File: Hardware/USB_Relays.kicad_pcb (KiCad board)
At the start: 2 copper layers, 90 parts, among them J1 282834-3, J10 282834-3, J11 282834-3, J12 282834-3, J13 282834-3, J14 282834-3, J15 282834-3, J16 282834-3, J17 DNP, J18 2411_06, J2 282834-3, J3 282834-3, J4 282834-3, J5 282834-3, J6 282834-3, J7 282834-3, J8 282834-3, J9 282834-3, K1 HRS1H-S_DC5V, K10 HRS1H-S_DC5V, K11 HRS1H-S_DC5V, K12 HRS1H-S_DC5V, K13 HRS1H-S_DC5V, K14 HRS1H-S_DC5V, K15 HRS1H-S_DC5V, K16 HRS1H-S_DC5V, K2 HRS1H-S_DC5V, K3 HRS1H-S_DC5V, K4 HRS1H-S_DC5V, K5 HRS1H-S_DC5V, K6 HRS1H-S_DC5V, K7 HRS1H-S_DC5V, K8 HRS1H-S_DC5V, K9 HRS1H-S_DC5V, Q1 BC848, Q10 BC848, Q11 BC848, Q12 BC848, Q13 BC848, Q14 BC848, Q15 BC848, Q16 BC848, Q2 BC848, Q3 BC848, Q4 BC848, Q5 BC848, Q6 BC848, Q7 BC848, Q8 BC848, Q9 BC848, U1 PIC16F18854-SO, U2 FT230XS

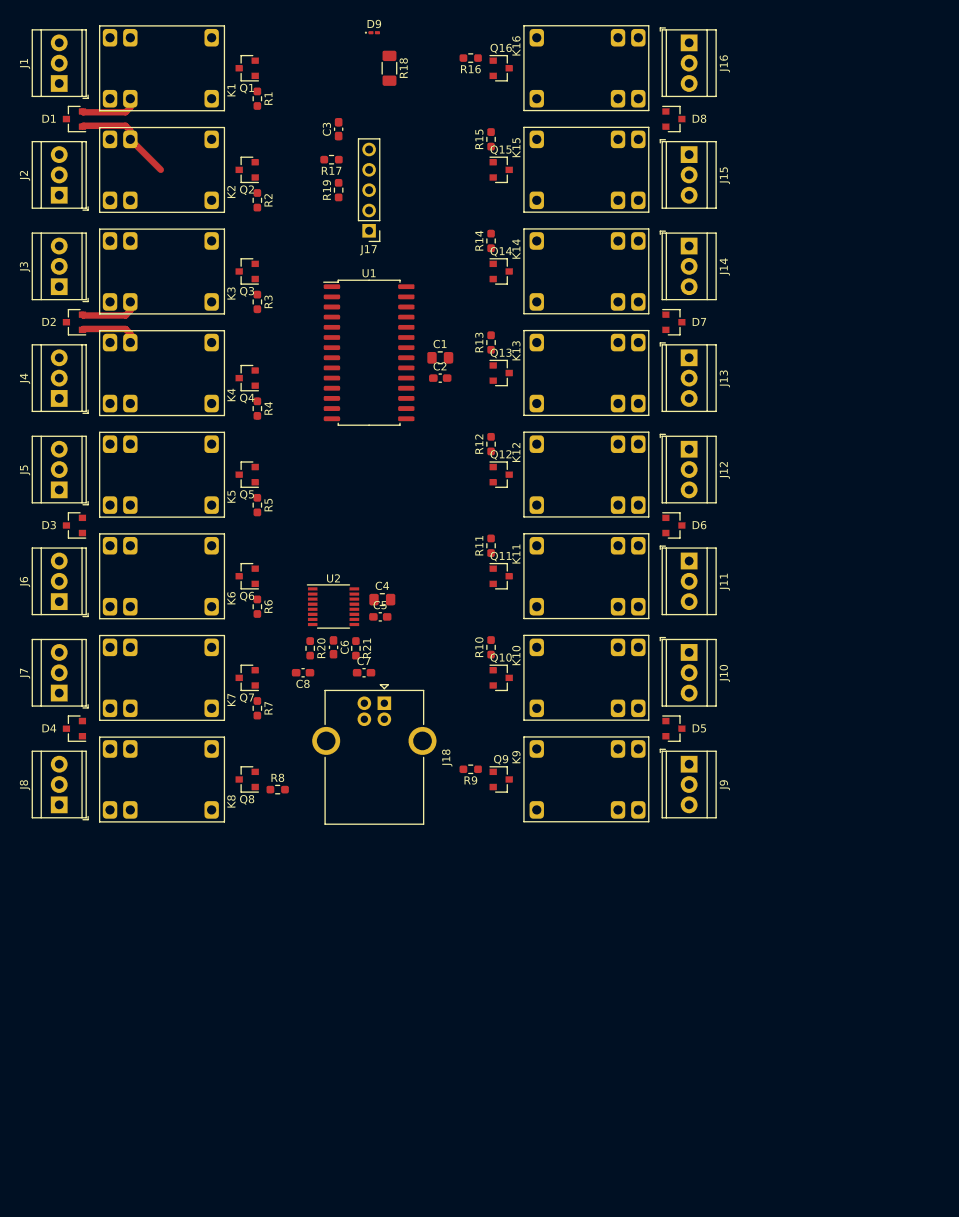
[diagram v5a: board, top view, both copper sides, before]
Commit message: [Hardware] Added mounting holes, PCB contour and ground planes.
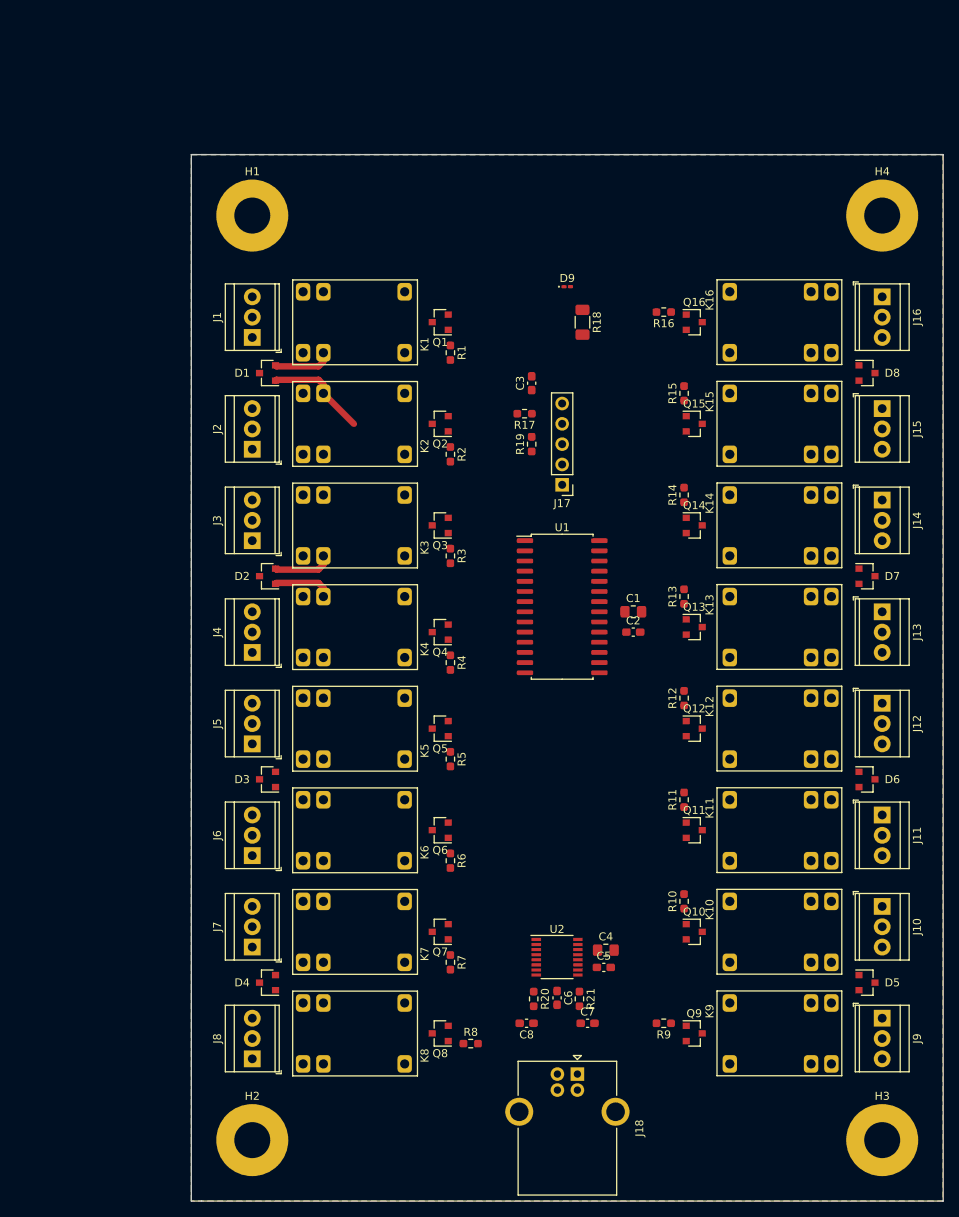
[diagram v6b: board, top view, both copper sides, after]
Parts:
- added H1: MountingHole_Pad, MountingHole:MountingHole_4.5mm_Pad, F.Cu at (45.7, 40.6)
- added H2: MountingHole_Pad, MountingHole:MountingHole_4.5mm_Pad, F.Cu at (45.7, 156.2)
- added H3: MountingHole_Pad, MountingHole:MountingHole_4.5mm_Pad, F.Cu at (124.5, 156.2)
- added H4: MountingHole_Pad, MountingHole:MountingHole_4.5mm_Pad, F.Cu at (124.5, 40.6)
- moved J18 52.3 mm to (86.4, 148.0)
- moved C4 52.0 mm to (89.9, 132.5)
- moved C5 52.0 mm to (89.7, 134.6)
- moved C6 52.0 mm to (83.8, 138.4)
- moved U2 52.0 mm to (83.8, 133.3)
- moved C7 52.0 mm to (87.6, 141.6)
- moved C8 52.0 mm to (80.0, 141.6)
- moved R20 52.0 mm to (80.9, 138.6)
- moved R21 52.0 mm to (86.6, 138.6)
- moved K10 39.9 mm to (111.8, 130.2)
- moved Q10 39.9 mm to (101.0, 130.2)
- moved J7 39.9 mm to (45.7, 132.1)
- moved J8 39.9 mm to (45.7, 146.1)
- moved K7 39.9 mm to (58.4, 130.2)
- moved Q7 39.9 mm to (69.2, 130.2)
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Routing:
- added copper zone on B.Cu, net GND
- added copper zone on F.Cu, net GND
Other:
- board outline added: 94 x 130.8 mm

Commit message: [Hardware] Routed whole PCB.
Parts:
- D9: footprint LED_SMD:LED_0201_0603Metric_Pad0.64x0.40mm_HandSolder -> LED_SMD:LED_0603_1608Metric_Pad1.05x0.95mm_HandSolder
- moved R13 6.63 mm to (97.8, 94.6), turned to 270 degrees
- moved C4 5.08 mm to (89.9, 127.4)
- moved C5 5.08 mm to (89.7, 129.5)
- moved C6 5.08 mm to (83.8, 133.3)
- moved C7 5.08 mm to (87.6, 136.5)
- moved C8 5.08 mm to (80.0, 136.5)
- moved R20 5.08 mm to (80.9, 133.5)
- moved R21 5.08 mm to (86.6, 133.5)
- moved U2 5.08 mm to (83.8, 128.3)
- moved R15 4.58 mm to (97.2, 66.7), turned to 270 degrees
- moved R5 4.32 mm to (72.5, 104.8), turned to 90 degrees
- moved R4 4.15 mm to (72.1, 92.7), turned to 90 degrees
- moved R12 4.13 mm to (96.8, 103.9), turned to 180 degrees
- moved R6 3.96 mm to (73.2, 118.4), turned to 0 degrees
- moved R7 3.87 mm to (73.0, 131.1), turned to 0 degrees
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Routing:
- net +5V: track 0.00 -> 686.7 mm, vias 0 -> 2
- net RELAY_8: track 0.00 -> 52.5 mm
- net RELAY_9: track 0.00 -> 47.8 mm
- net RELAY_7: track 0.00 -> 43.9 mm
- net RELAY_14: track 0.00 -> 39.7 mm, vias 0 -> 2
- net FTDI_RX: track 0.00 -> 39.4 mm, vias 0 -> 2
- net Net-(R18-Pad2): track 0.00 -> 39.1 mm, vias 0 -> 2
- net FTDI_TX: track 0.00 -> 38.9 mm, vias 0 -> 2
- net RELAY_10: track 0.00 -> 38.8 mm
- net RELAY_16: track 0.00 -> 36.6 mm
- net RELAY_11: track 0.00 -> 34.2 mm
- net RELAY_6: track 0.00 -> 33.6 mm
- net RELAY_1: track 0.00 -> 30.1 mm
- net RELAY_15: track 0.00 -> 25.5 mm
- net Net-(D7-Pad2): track 0.00 -> 22.6 mm
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- added copper zone on F.Cu, net +3.3VA
- added copper zone on F.Cu, net +5V

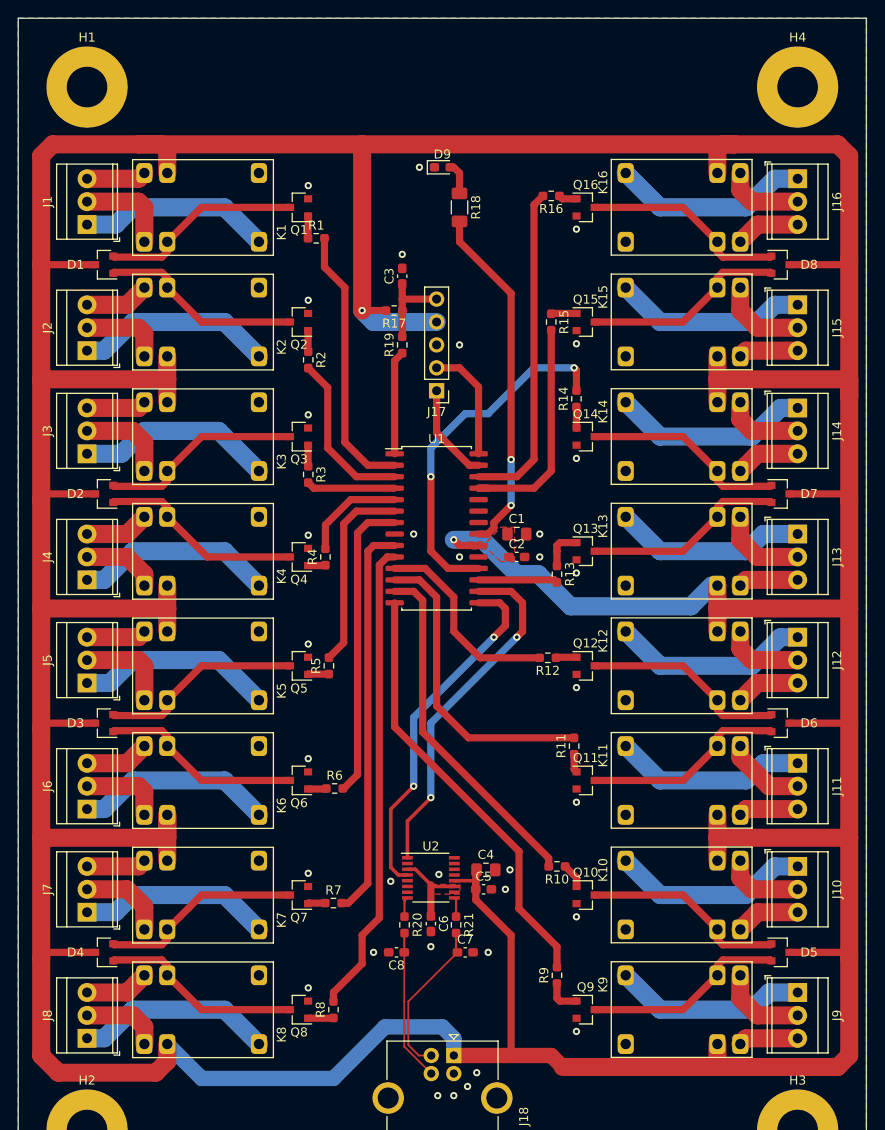
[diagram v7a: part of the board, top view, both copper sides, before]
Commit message: [Hardware] Moved LED to make it more visible, cleaned components designation positions, added information about connectors pins to the PCB.
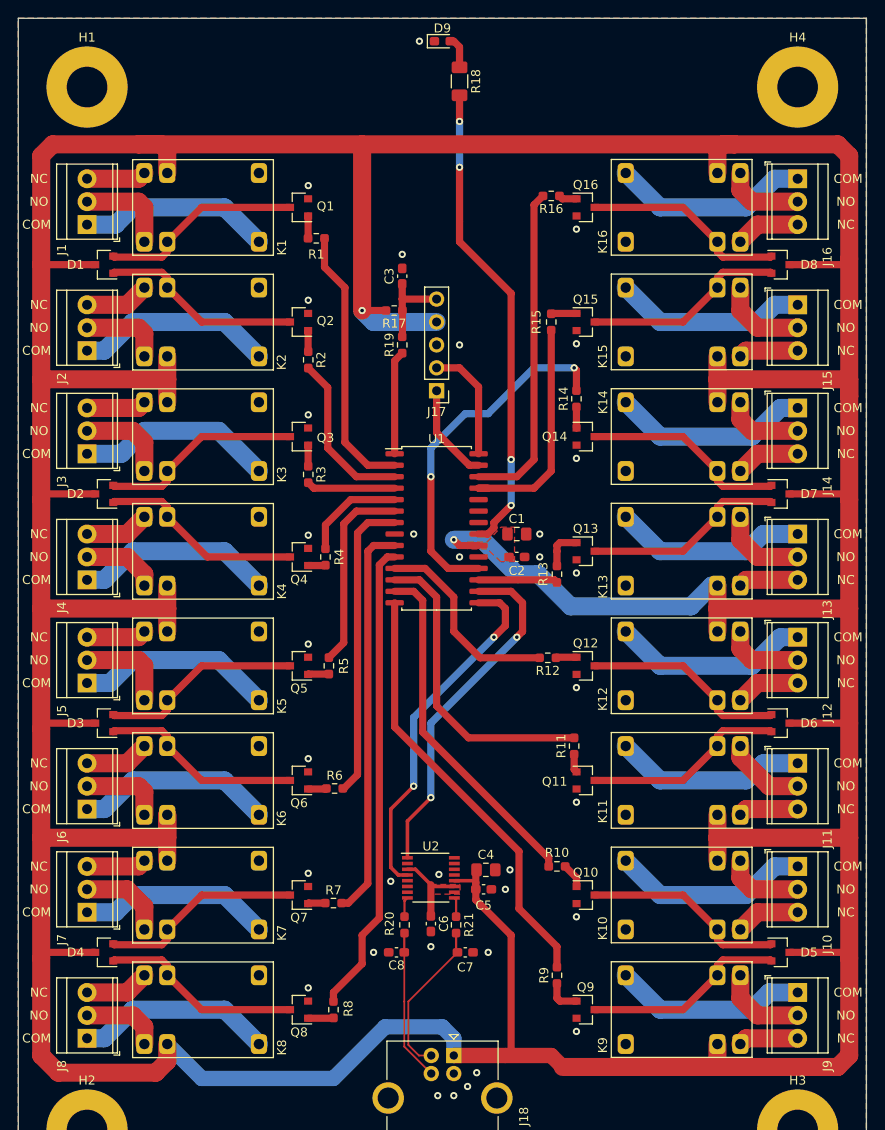
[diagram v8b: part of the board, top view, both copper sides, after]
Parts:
- moved D9 14.0 mm to (85.1, 35.6)
- moved R18 14.0 mm to (87.0, 40.0)
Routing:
- net Net-(R18-Pad2): track 39.1 -> 53.1 mm, vias 2 -> 4
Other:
- board text added: "14/08/2021"
- board text added: "COM"
- board text added: "NC"
- board text added: "NO"
